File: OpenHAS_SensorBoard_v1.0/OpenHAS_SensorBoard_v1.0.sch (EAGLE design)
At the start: 18 parts, among them IC1 MCP1703CB, IC2 MCP9700SMD, IC3 TEMT6000, IC4 HIH-5030SMD, Q1 N-MOSFET

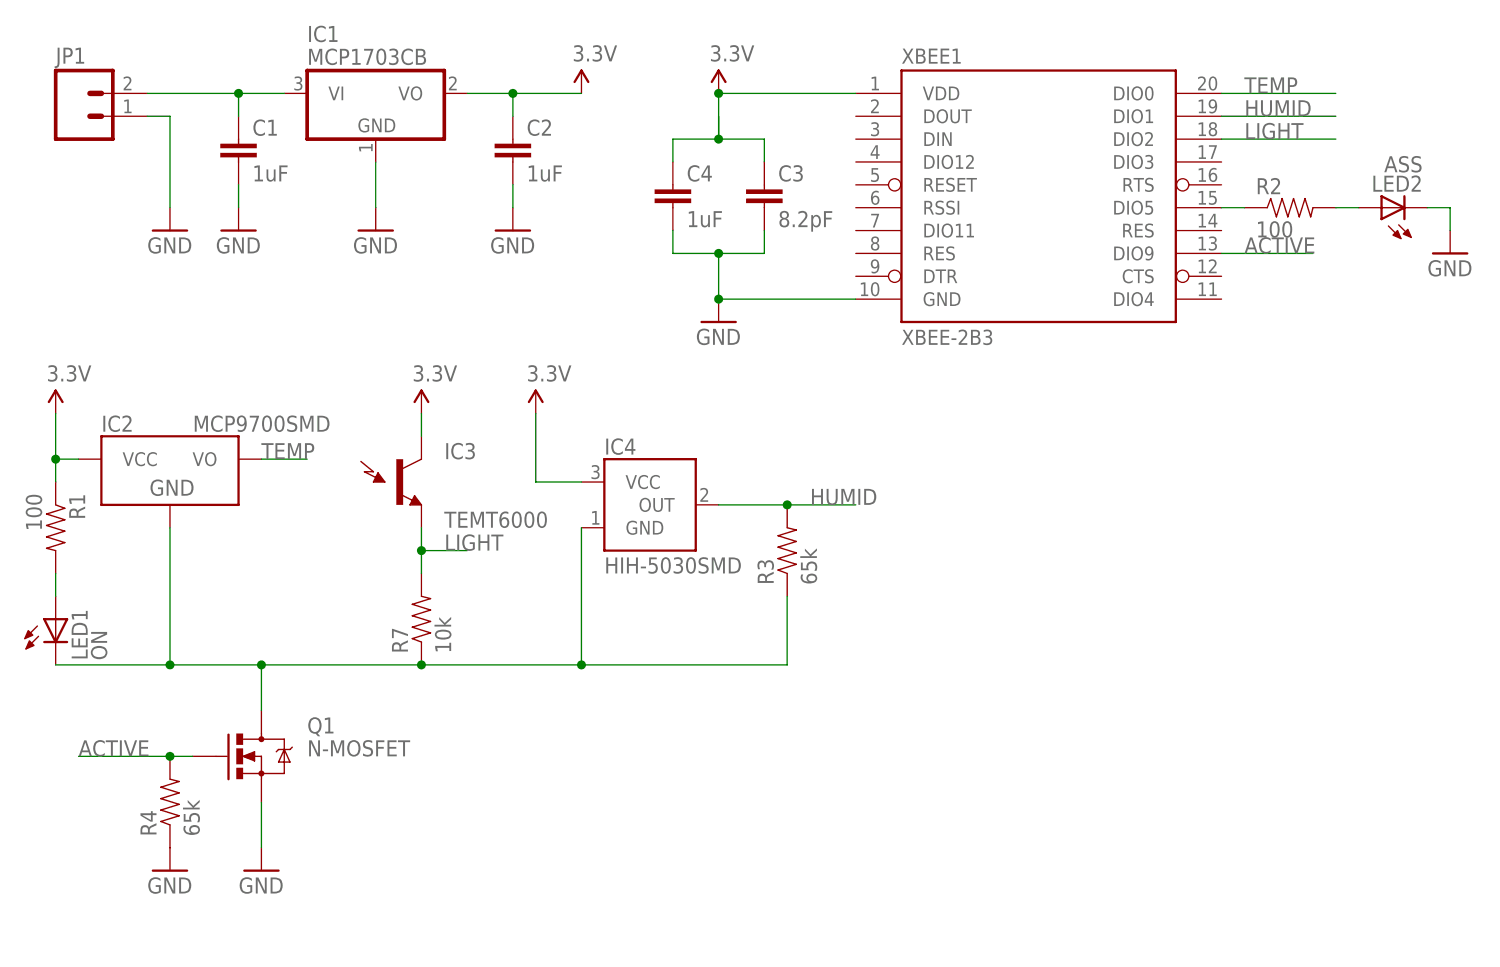
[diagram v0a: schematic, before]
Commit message: Added voltage divider to the humidity sensor. Redesigned layout
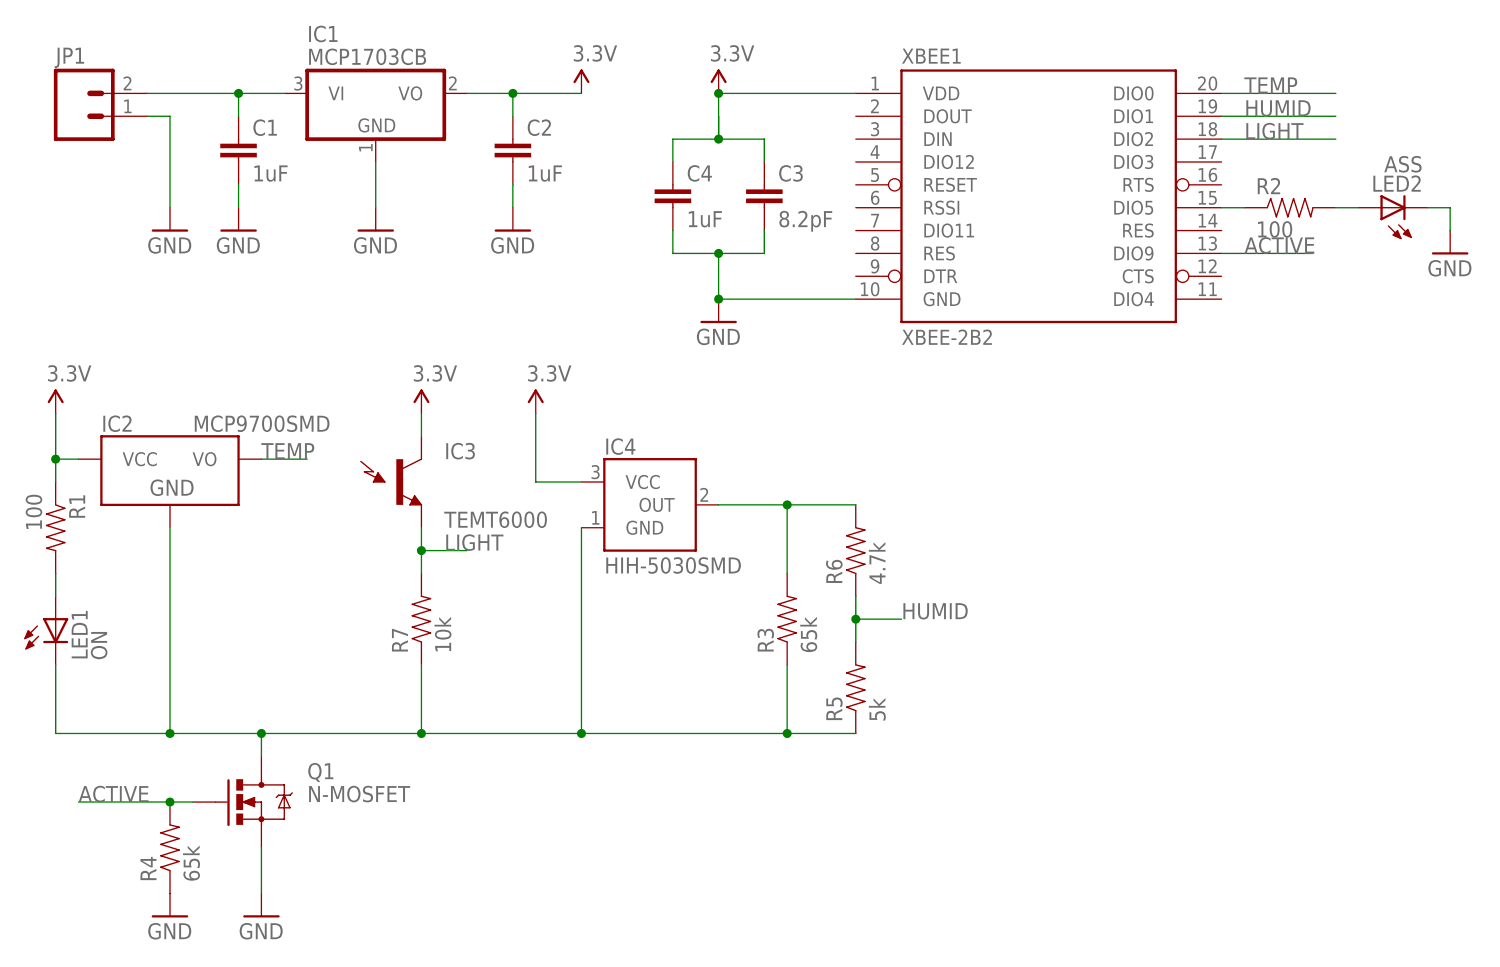
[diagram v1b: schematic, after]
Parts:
- added R5: 5k, SparkFun-Resistors:RESISTOR0805-RES
- added R6: 4.7k, SparkFun-Resistors:RESISTOR0805-RES
- XBEE1: value XBEE-2B3 -> XBEE-2B2; device SparkFun-RF:XBEE-2B3 -> SparkFun-RF:XBEE-2B2
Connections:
- new net N$3: IC4.OUT, R3.2, R6.2
- net HUMID: now also R5.2, R6.1; no longer IC4.OUT, R3.2
- net SW_GND: now also R5.1
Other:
- moved on the sheet: Q1, R3, R4
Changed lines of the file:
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@@
 </classes>
 <parts>
-<part name="XBEE1" library="SparkFun-RF" deviceset="XBEE-2" device="B3"/>
+<part name="XBEE1" library="SparkFun-RF" deviceset="XBEE-2" device="B2" value="XBEE-2B2"/>
 <part name="IC2" library="SparkFun-Sensors" deviceset="MCP9700" device="SMD"/>
 <part name="IC1" library="linear" deviceset="MCP1703" device="CB"/>
@@
 <part name="GND6" library="SparkFun-Aesthetics" deviceset="GND" device=""/>
 <part name="GND8" library="SparkFun-Aesthetics" deviceset="GND" device=""/>
+<part name="R5" library="SparkFun-Resistors" deviceset="RESISTOR" device="0805-RES" value="5k"/>
+<part name="R6" library="SparkFun-Resistors" deviceset="RESISTOR" device="0805-RES" value="4.7k"/>
 </parts>
 <sheets>
@@
 <instance part="SUPPLY8" gate="G$1" x="66.04" y="43.18"/>
 <instance part="R7" gate="G$1" x="66.04" y="20.32" rot="R90"/>
-<instance part="R3" gate="G$1" x="106.68" y="27.94" rot="R90"/>
-<instance part="Q1" gate="G$1" x="48.26" y="5.08"/>
-<instance part="R4" gate="G$1" x="38.1" y="0" rot="R90"/>
-<instance part="GND3" gate="1" x="38.1" y="-7.62"/>
-<instance part="GND4" gate="1" x="48.26" y="-7.62"/>
+<instance part="R3" gate="G$1" x="106.68" y="20.32" rot="R90"/>
+<instance part="Q1" gate="G$1" x="48.26" y="0"/>
+<instance part="R4" gate="G$1" x="38.1" y="-5.08" rot="R90"/>
+<instance part="GND3" gate="1" x="38.1" y="-12.7"/>
+<instance part="GND4" gate="1" x="48.26" y="-12.7"/>
 <instance part="R2" gate="G$1" x="162.56" y="66.04"/>
 <instance part="LED2" gate="G$1" x="172.72" y="66.04" rot="R90"/>
 <instance part="GND6" gate="1" x="180.34" y="60.96"/>
 <instance part="GND8" gate="1" x="38.1" y="63.5"/>
+<instance part="R5" gate="G$1" x="114.3" y="12.7" rot="R90"/>
+<instance part="R6" gate="G$1" x="114.3" y="27.94" rot="R90"/>
 </instances>
 <busses>
@@
 <pinref part="Q1" gate="G$1" pin="S"/>
 <pinref part="GND4" gate="1" pin="GND"/>
-<wire x1="48.26" y1="0" x2="48.26" y2="-5.08" width="0.1524" layer="91"/>
+<wire x1="48.26" y1="-5.08" x2="48.26" y2="-10.16" width="0.1524" layer="91"/>
 </segment>
 <segment>
@@
 <pinref part="Q1" gate="G$1" pin="G"/>
 <pinref part="R4" gate="G$1" pin="2"/>
-<wire x1="40.64" y1="5.08" x2="38.1" y2="5.08" width="0.1524" layer="91"/>
-<wire x1="38.1" y1="5.08" x2="27.94" y2="5.08" width="0.1524" layer="91"/>
-<junction x="38.1" y="5.08"/>
-<label x="27.94" y="5.08" size="1.778" layer="95"/>
+<wire x1="40.64" y1="0" x2="38.1" y2="0" width="0.1524" layer="91"/>
+<wire x1="38.1" y1="0" x2="27.94" y2="0" width="0.1524" layer="91"/>
+<junction x="38.1" y="0"/>
+<label x="27.94" y="0" size="1.778" layer="95"/>
 </segment>
 </net>
@@
 </segment>
 <segment>
-<pinref part="IC4" gate="G$1" pin="OUT"/>
-<pinref part="R3" gate="G$1" pin="2"/>
-<wire x1="99.06" y1="33.02" x2="106.68" y2="33.02" width="0.1524" layer="91"/>
-<wire x1="106.68" y1="33.02" x2="114.3" y2="33.02" width="0.1524" layer="91"/>
-<junction x="106.68" y="33.02"/>
-<label x="109.22" y="33.02" size="1.778" layer="95"/>
+<pinref part="R6" gate="G$1" pin="1"/>
+<pinref part="R5" gate="G$1" pin="2"/>
+<wire x1="114.3" y1="22.86" x2="114.3" y2="20.32" width="0.1524" layer="91"/>
+<wire x1="114.3" y1="20.32" x2="114.3" y2="17.78" width="0.1524" layer="91"/>
+<wire x1="114.3" y1="20.32" x2="119.38" y2="20.32" width="0.1524" layer="91"/>
+<junction x="114.3" y="20.32"/>
+<label x="119.38" y="20.32" size="1.778" layer="95"/>
 </segment>
 </net>
@@
 <net name="SW_GND" class="0">
 <segment>
+<pinref part="IC4" gate="G$1" pin="GND"/>
+<wire x1="83.82" y1="7.62" x2="83.82" y2="30.48" width="0.1524" layer="91"/>
+<pinref part="R3" gate="G$1" pin="1"/>
+<wire x1="106.68" y1="15.24" x2="106.68" y2="7.62" width="0.1524" layer="91"/>
+<wire x1="106.68" y1="7.62" x2="83.82" y2="7.62" width="0.1524" layer="91"/>
+<pinref part="R5" gate="G$1" pin="1"/>
+<wire x1="114.3" y1="7.62" x2="106.68" y2="7.62" width="0.1524" layer="91"/>
+<junction x="106.68" y="7.62"/>
+<pinref part="IC2" gate="G$1" pin="GND"/>
+<wire x1="38.1" y1="30.48" x2="38.1" y2="7.62" width="0.1524" layer="91"/>
 <pinref part="Q1" gate="G$1" pin="D"/>
-<pinref part="IC4" gate="G$1" pin="GND"/>
-<wire x1="83.82" y1="15.24" x2="83.82" y2="30.48" width="0.1524" layer="91"/>
+<wire x1="48.26" y1="5.08" x2="48.26" y2="7.62" width="0.1524" layer="91"/>
+<wire x1="48.26" y1="7.62" x2="38.1" y2="7.62" width="0.1524" layer="91"/>
+<wire x1="83.82" y1="7.62" x2="66.04" y2="7.62" width="0.1524" layer="91"/>
+<junction x="83.82" y="7.62"/>
+<junction x="48.26" y="7.62"/>
 <pinref part="R7" gate="G$1" pin="1"/>
-<wire x1="66.04" y1="15.24" x2="83.82" y2="15.24" width="0.1524" layer="91"/>
-<pinref part="IC2" gate="G$1" pin="GND"/>
-<wire x1="38.1" y1="30.48" x2="38.1" y2="15.24" width="0.1524" layer="91"/>
-<wire x1="66.04" y1="15.24" x2="48.26" y2="15.24" width="0.1524" layer="91"/>
-<junction x="66.04" y="15.24"/>
-<wire x1="48.26" y1="15.24" x2="38.1" y2="15.24" width="0.1524" layer="91"/>
-<wire x1="48.26" y1="10.16" x2="48.26" y2="15.24" width="0.1524" layer="91"/>
-<junction x="48.26" y="15.24"/>
-<pinref part="R3" gate="G$1" pin="1"/>
-<wire x1="106.68" y1="22.86" x2="106.68" y2="15.24" width="0.1524" layer="91"/>
-<wire x1="106.68" y1="15.24" x2="83.82" y2="15.24" width="0.1524" layer="91"/>
-<junction x="83.82" y="15.24"/>
+<wire x1="66.04" y1="7.62" x2="48.26" y2="7.62" width="0.1524" layer="91"/>
+<wire x1="66.04" y1="15.24" x2="66.04" y2="7.62" width="0.1524" layer="91"/>
+<junction x="66.04" y="7.62"/>
 <pinref part="LED1" gate="G$1" pin="C"/>
-<wire x1="38.1" y1="15.24" x2="25.4" y2="15.24" width="0.1524" layer="91"/>
-<junction x="38.1" y="15.24"/>
+<wire x1="25.4" y1="15.24" x2="25.4" y2="7.62" width="0.1524" layer="91"/>
+<wire x1="25.4" y1="7.62" x2="38.1" y2="7.62" width="0.1524" layer="91"/>
+<junction x="38.1" y="7.62"/>
 </segment>
 </net>
@@
 </segment>
 </net>
+<net name="N$3" class="0">
+<segment>
+<pinref part="R6" gate="G$1" pin="2"/>
+<pinref part="IC4" gate="G$1" pin="OUT"/>
+<wire x1="114.3" y1="33.02" x2="106.68" y2="33.02" width="0.1524" layer="91"/>
+<pinref part="R3" gate="G$1" pin="2"/>
+<wire x1="106.68" y1="33.02" x2="99.06" y2="33.02" width="0.1524" layer="91"/>
+<wire x1="106.68" y1="25.4" x2="106.68" y2="33.02" width="0.1524" layer="91"/>
+<junction x="106.68" y="33.02"/>
+</segment>
+</net>
